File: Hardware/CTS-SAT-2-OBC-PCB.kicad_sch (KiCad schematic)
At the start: 0 parts

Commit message: Small updates
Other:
- removed sheet Temperature Sensor
- sheet STM32 ports: added none; removed DEBUG_LED, I2C4_SCL, I2C4_SDA
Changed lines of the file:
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@@
-	(wire
-		(pts
-			(xy 203.2 101.6) (xy 214.63 101.6)
-		)
-		(stroke
-			(width 0)
-			(type default)
-		)
-	)
 	(wire
 		(pts
@@
 		(pts
 			(xy 203.2 78.74) (xy 248.92 78.74)
-		)
-		(stroke
-			(width 0)
-			(type default)
-		)
-	)
-	(wire
-		(pts
-			(xy 203.2 99.06) (xy 214.63 99.06)
 		)
 		(stroke
@@
 	)
 	(sheet
-		(at 214.63 91.44)
-		(size 20.32 19.05)
-		(exclude_from_sim no)
-		(in_bom yes)
-		(on_board yes)
-		(dnp no)
-		(fields_autoplaced yes)
-		(stroke
-			(width 0.1524)
-			(type solid)
-		)
-		(fill
-			(color 0 0 0 0.0000)
-		)
-		(property "Sheetname" "Temperature Sensor"
-			(at 214.63 90.7284 0)
-			(effects
-				(font
-					(size 1.27 1.27)
-				)
-				(justify left bottom)
-			)
-		)
-		(property "Sheetfile" "temperature_sensor.kicad_sch"
-			(at 214.63 111.0746 0)
-			(effects
-				(font
-					(size 1.27 1.27)
-				)
-				(justify left top)
-			)
-		)
-		(pin "TEMP_SENS_SDA" bidirectional
-			(at 214.63 99.06 180)
-			(effects
-				(font
-					(size 1.27 1.27)
-				)
-				(justify left)
-			)
-		)
-		(pin "TEMP_SENS_SCL" bidirectional
-			(at 214.63 101.6 180)
-			(effects
-				(font
-					(size 1.27 1.27)
-				)
-				(justify left)
-			)
-		)
-		(instances
-			(project "CTS-SAT-2-OBC-PCB"
-				(path "/58243925-df8d-4fc1-899e-fce866d1d25a"
-					(page "5")
-				)
-			)
-		)
-	)
-	(sheet
 		(at 248.92 67.31)
 		(size 30.48 27.94)
@@
 			)
 		)
-		(pin "I2C4_SCL" bidirectional
-			(at 203.2 101.6 0)
-			(effects
-				(font
-					(size 1.27 1.27)
-				)
-				(justify right)
-			)
-		)
-		(pin "I2C4_SDA" bidirectional
-			(at 203.2 99.06 0)
-			(effects
-				(font
-					(size 1.27 1.27)
-				)
-				(justify right)
-			)
-		)
 		(pin "SPI2_MOSI" bidirectional
 			(at 144.78 99.06 180)
@@
 			(effects
 				(font
-					(size 1.27 1.27)
-				)
-				(justify left)
-			)
-		)
-		(pin "DEBUG_LED" output
-			(at 144.78 132.08 180)
-			(effects
-				(font

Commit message: RP2040 Schematic
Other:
- sheet PC104 Headers ports: added none; removed V_BAT
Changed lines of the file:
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@@
-			)
-		)
-		(pin "V_BAT" input
-			(at 279.4 90.17 0)
-			(effects
-				(font
-					(size 1.27 1.27)
-				)
-				(justify right)
 			)
 		)

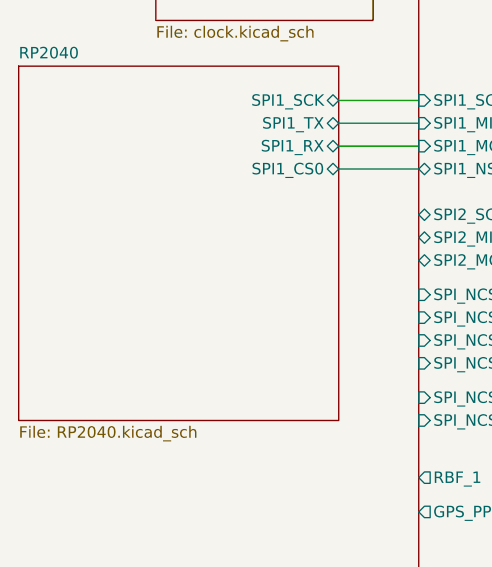
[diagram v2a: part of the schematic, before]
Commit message: Add fast clock
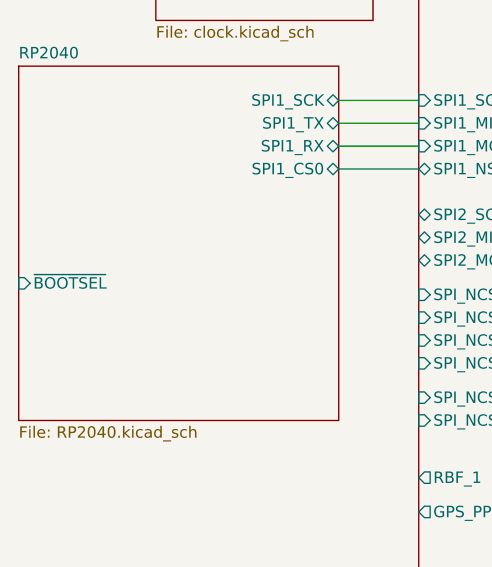
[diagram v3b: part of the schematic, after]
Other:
- sheet RP2040 ports: added ~{BOOTSEL}; removed none
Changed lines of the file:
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@@
+			)
+		)
+		(pin "~{BOOTSEL}" input
+			(at 100.33 101.6 180)
+			(effects
+				(font
+					(size 1.27 1.27)
+				)
+				(justify left)
 			)
 		)

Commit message: minor fix
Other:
- removed sheet Clock
- sheet STM32 ports: added none; removed BOOT0, OSC_IN
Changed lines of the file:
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@@
-	(wire
-		(pts
-			(xy 139.7 64.77) (xy 144.78 64.77)
-		)
-		(stroke
-			(width 0)
-			(type default)
-		)
-	)
 	(wire
 		(pts
@@
 			(width 0)
 			(type default)
-		)
-	)
-	(wire
-		(pts
-			(xy 139.7 62.23) (xy 144.78 62.23)
-		)
-		(stroke
-			(width 0)
-			(type default)
-		)
-	)
-	(sheet
-		(at 115.57 55.88)
-		(size 24.13 16.51)
-		(exclude_from_sim no)
-		(in_bom yes)
-		(on_board yes)
-		(dnp no)
-		(fields_autoplaced yes)
-		(stroke
-			(width 0.1524)
-			(type solid)
-		)
-		(fill
-			(color 0 0 0 0.0000)
-		)
-		(property "Sheetname" "Clock"
-			(at 115.57 55.1684 0)
-			(effects
-				(font
-					(size 1.27 1.27)
-				)
-				(justify left bottom)
-			)
-		)
-		(property "Sheetfile" "clock.kicad_sch"
-			(at 115.57 72.9746 0)
-			(effects
-				(font
-					(size 1.27 1.27)
-				)
-				(justify left top)
-			)
-		)
-		(pin "BOOT0" output
-			(at 139.7 62.23 0)
-			(effects
-				(font
-					(size 1.27 1.27)
-				)
-				(justify right)
-			)
-		)
-		(pin "OSC_IN" output
-			(at 139.7 64.77 0)
-			(effects
-				(font
-					(size 1.27 1.27)
-				)
-				(justify right)
-			)
-		)
-		(pin "OSC32_IN" output
-			(at 139.7 67.31 0)
-			(effects
-				(font
-					(size 1.27 1.27)
-				)
-				(justify right)
-			)
-		)
-		(pin "NRST" output
-			(at 139.7 59.69 0)
-			(effects
-				(font
-					(size 1.27 1.27)
-				)
-				(justify right)
-			)
-		)
-		(instances
-			(project "CTS-SAT-2-OBC-PCB"
-				(path "/58243925-df8d-4fc1-899e-fce866d1d25a"
-					(page "6")
-				)
-			)
 		)
 	)
@@
 			)
 		)
-		(pin "BOOT0" input
-			(at 144.78 62.23 180)
-			(effects
-				(font
-					(size 1.27 1.27)
-				)
-				(justify left)
-			)
-		)
 		(pin "NRST" input
 			(at 144.78 59.69 180)
@@
 			(effects
 				(font
-					(size 1.27 1.27)
-				)
-				(justify left)
-			)
-		)
-		(pin "OSC_IN" input
-			(at 144.78 64.77 180)
-			(effects
-				(font

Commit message: STM32 RTC
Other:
- added sheet Flash Memory (stm32_flash.kicad_sch)
- sheet STM32 ports: added none; removed OSC32_IN
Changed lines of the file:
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@@
+	(wire
+		(pts
+			(xy 130.81 102.87) (xy 144.78 102.87)
+		)
+		(stroke
+			(width 0)
+			(type default)
+		)
+	)
 	(wire
 		(pts
@@
 	(wire
 		(pts
+			(xy 130.81 105.41) (xy 144.78 105.41)
+		)
+		(stroke
+			(width 0)
+			(type default)
+		)
+	)
+	(wire
+		(pts
 			(xy 138.43 168.91) (xy 288.29 168.91)
 		)
@@
 	(wire
 		(pts
-			(xy 135.89 88.9) (xy 144.78 88.9)
+			(xy 97.79 81.28) (xy 144.78 81.28)
+		)
+		(stroke
+			(width 0)
+			(type default)
+		)
+	)
+	(wire
+		(pts
+			(xy 130.81 110.49) (xy 144.78 110.49)
 		)
 		(stroke
@@
 	(wire
 		(pts
-			(xy 135.89 86.36) (xy 144.78 86.36)
-		)
-		(stroke
-			(width 0)
-			(type default)
-		)
-	)
-	(wire
-		(pts
-			(xy 139.7 67.31) (xy 144.78 67.31)
-		)
-		(stroke
-			(width 0)
-			(type default)
-		)
-	)
-	(wire
-		(pts
-			(xy 135.89 81.28) (xy 144.78 81.28)
+			(xy 97.79 78.74) (xy 144.78 78.74)
+		)
+		(stroke
+			(width 0)
+			(type default)
+		)
+	)
+	(wire
+		(pts
+			(xy 97.79 73.66) (xy 144.78 73.66)
 		)
 		(stroke
@@
 	(wire
 		(pts
-			(xy 135.89 83.82) (xy 144.78 83.82)
+			(xy 130.81 107.95) (xy 144.78 107.95)
+		)
+		(stroke
+			(width 0)
+			(type default)
+		)
+	)
+	(wire
+		(pts
+			(xy 97.79 76.2) (xy 144.78 76.2)
 		)
 		(stroke
@@
 			(width 0)
 			(type default)
+		)
+	)
+	(wire
+		(pts
+			(xy 130.81 96.52) (xy 144.78 96.52)
+		)
+		(stroke
+			(width 0)
+			(type default)
+		)
+	)
+	(wire
+		(pts
+			(xy 130.81 93.98) (xy 144.78 93.98)
+		)
+		(stroke
+			(width 0)
+			(type default)
+		)
+	)
+	(wire
+		(pts
+			(xy 130.81 99.06) (xy 144.78 99.06)
+		)
+		(stroke
+			(width 0)
+			(type default)
+		)
+	)
+	(sheet
+		(at 109.22 91.44)
+		(size 21.59 22.86)
+		(exclude_from_sim no)
+		(in_bom yes)
+		(on_board yes)
+		(dnp no)
+		(fields_autoplaced yes)
+		(stroke
+			(width 0.1524)
+			(type solid)
+		)
+		(fill
+			(color 0 0 0 0.0000)
+		)
+		(property "Sheetname" "Flash Memory"
+			(at 109.22 90.7284 0)
+			(effects
+				(font
+					(size 1.27 1.27)
+				)
+				(justify left bottom)
+			)
+		)
+		(property "Sheetfile" "stm32_flash.kicad_sch"
+			(at 109.22 114.8846 0)
+			(effects
+				(font
+					(size 1.27 1.27)
+				)
+				(justify left top)
+				(hide yes)
+			)
+		)
+		(pin "SPI_NCS_FLASH_3" input
+			(at 130.81 110.49 0)
+			(effects
+				(font
+					(size 1.27 1.27)
+				)
+				(justify right)
+			)
+		)
+		(pin "SPI_FLASH_MISO" output
+			(at 130.81 96.52 0)
+			(effects
+				(font
+					(size 1.27 1.27)
+				)
+				(justify right)
+			)
+		)
+		(pin "SPI_NCS_FLASH_1" input
+			(at 130.81 105.41 0)
+			(effects
+				(font
+					(size 1.27 1.27)
+				)
+				(justify right)
+			)
+		)
+		(pin "SPI_FLASH_SCLK" output
+			(at 130.81 93.98 0)
+			(effects
+				(font
+					(size 1.27 1.27)
+				)
+				(justify right)
+			)
+		)
+		(pin "SPI_NCS_FLASH_2" input
+			(at 130.81 107.95 0)
+			(effects
+				(font
+					(size 1.27 1.27)
+				)
+				(justify right)
+			)
+		)
+		(pin "SPI_FLASH_MOSI" output
+			(at 130.81 99.06 0)
+			(effects
+				(font
+					(size 1.27 1.27)
+				)
+				(justify right)
+			)
+		)
+		(pin "SPI_NCS_FLASH_0" input
+			(at 130.81 102.87 0)
+			(effects
+				(font
+					(size 1.27 1.27)
+				)
+				(justify right)
+			)
+		)
+		(instances
+			(project "CTS-SAT-2-OBC-PCB"
+				(path "/58243925-df8d-4fc1-899e-fce866d1d25a"
+					(page "5")
+				)
+			)
 		)
 	)
@@
 	)
 	(sheet
-		(at 100.33 77.47)
-		(size 35.56 39.37)
+		(at 62.23 66.04)
+		(size 35.56 21.59)
 		(exclude_from_sim no)
 		(in_bom yes)
@@
 		)
 		(property "Sheetname" "RP2040"
-			(at 100.33 76.7584 0)
+			(at 62.23 65.3284 0)
 			(effects
 				(font
@@
 		)
 		(property "Sheetfile" "RP2040.kicad_sch"
-			(at 100.33 117.4246 0)
+			(at 62.23 88.2146 0)
 			(effects
 				(font
@@
 				)
 				(justify left top)
+				(hide yes)
 			)
 		)
 		(pin "SPI1_RX" bidirectional
-			(at 135.89 86.36 0)
+			(at 97.79 78.74 0)
 			(effects
 				(font
@@
 		)
 		(pin "SPI1_CS0" bidirectional
-			(at 135.89 88.9 0)
+			(at 97.79 81.28 0)
 			(effects
 				(font
@@
 		)
 		(pin "SPI1_TX" bidirectional
-			(at 135.89 83.82 0)
+			(at 97.79 76.2 0)
 			(effects
 				(font
@@
 		)
 		(pin "SPI1_SCK" bidirectional
-			(at 135.89 81.28 0)
+			(at 97.79 73.66 0)
 			(effects
 				(font
@@
 		)
 		(pin "~{BOOTSEL}" input
-			(at 100.33 101.6 180)
+			(at 62.23 72.39 180)
 			(effects
 				(font
@@
 		)
 		(pin "SPI1_MOSI" input
-			(at 144.78 86.36 180)
+			(at 144.78 78.74 180)
 			(effects
 				(font
@@
 		)
 		(pin "SPI1_MISO" input
-			(at 144.78 83.82 180)
+			(at 144.78 76.2 180)
 			(effects
 				(font
@@
 		)
 		(pin "SPI1_SCLK" input
-			(at 144.78 81.28 180)
+			(at 144.78 73.66 180)
 			(effects
 				(font
@@
 			)
 		)
-		(pin "OSC32_IN" input
-			(at 144.78 67.31 180)
-			(effects
-				(font
-					(size 1.27 1.27)
-				)
-				(justify left)
-			)
-		)
 		(pin "SPI1_NSS" bidirectional
-			(at 144.78 88.9 180)
-			(effects
-				(font
+			(at 144.78 81.28 180)
+			(effects
+				(font

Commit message: prepare for FRAM
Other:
- sheet Flash Memory renamed Memory
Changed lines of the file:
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@@
 			(color 0 0 0 0.0000)
 		)
-		(property "Sheetname" "Flash Memory"
+		(property "Sheetname" "Memory"
 			(at 109.22 90.7284 0)
 			(effects
@@
 		)
 		(pin "BOOM_CTRL_1" output
-			(at 144.78 140.97 180)
+			(at 144.78 143.51 180)
 			(effects
 				(font
@@
 		)
 		(pin "BOOM_CTRL_2" output
-			(at 144.78 143.51 180)
-			(effects
-				(font
+			(at 144.78 146.05 180)
+			(effects
+				(font

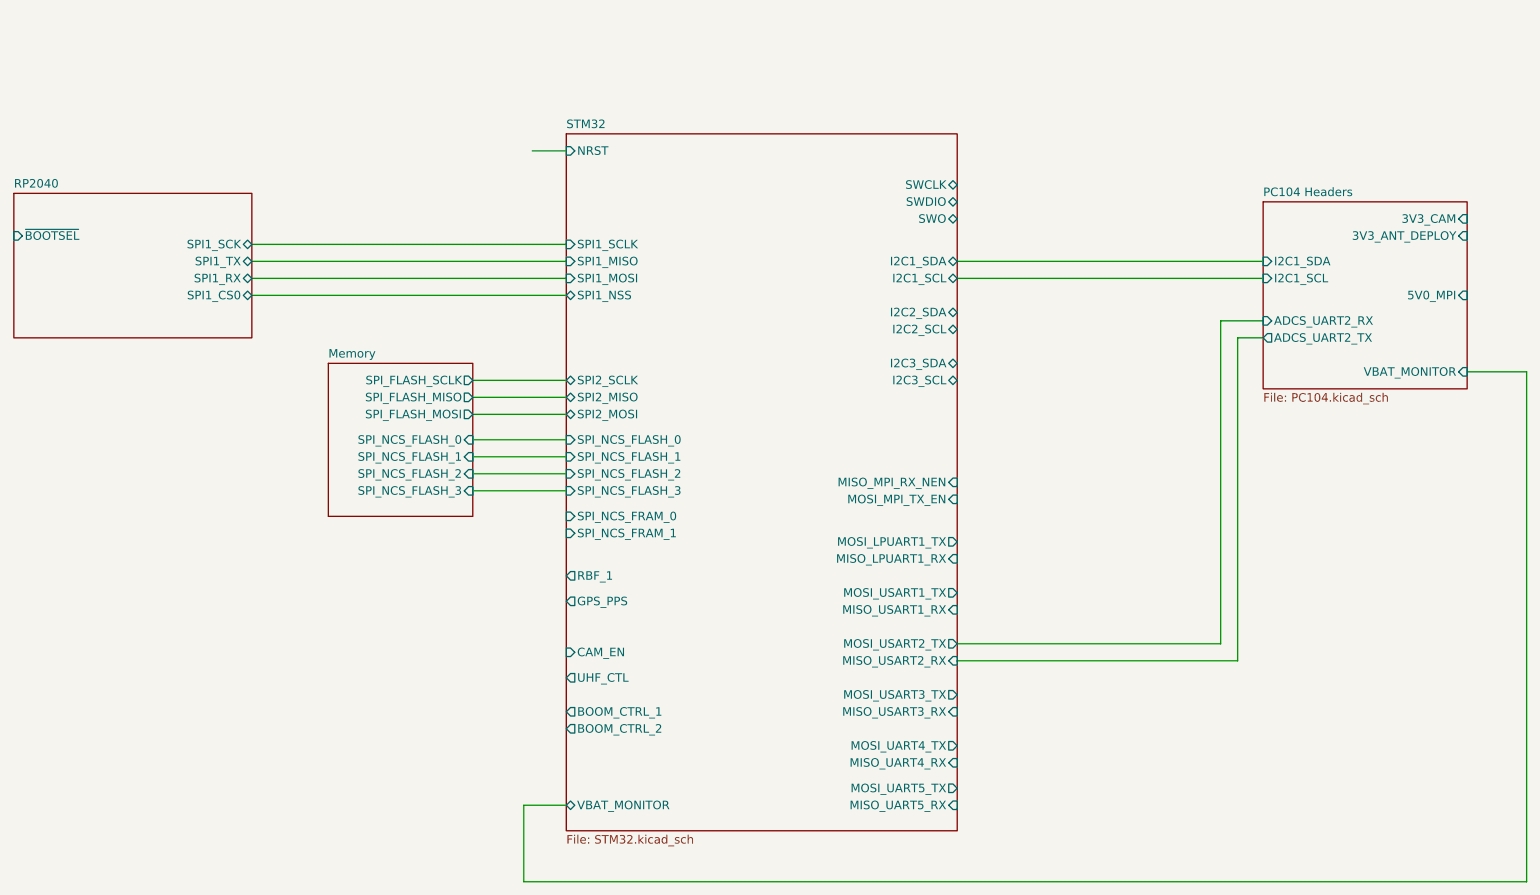
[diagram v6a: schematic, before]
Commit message: Begin with connectors
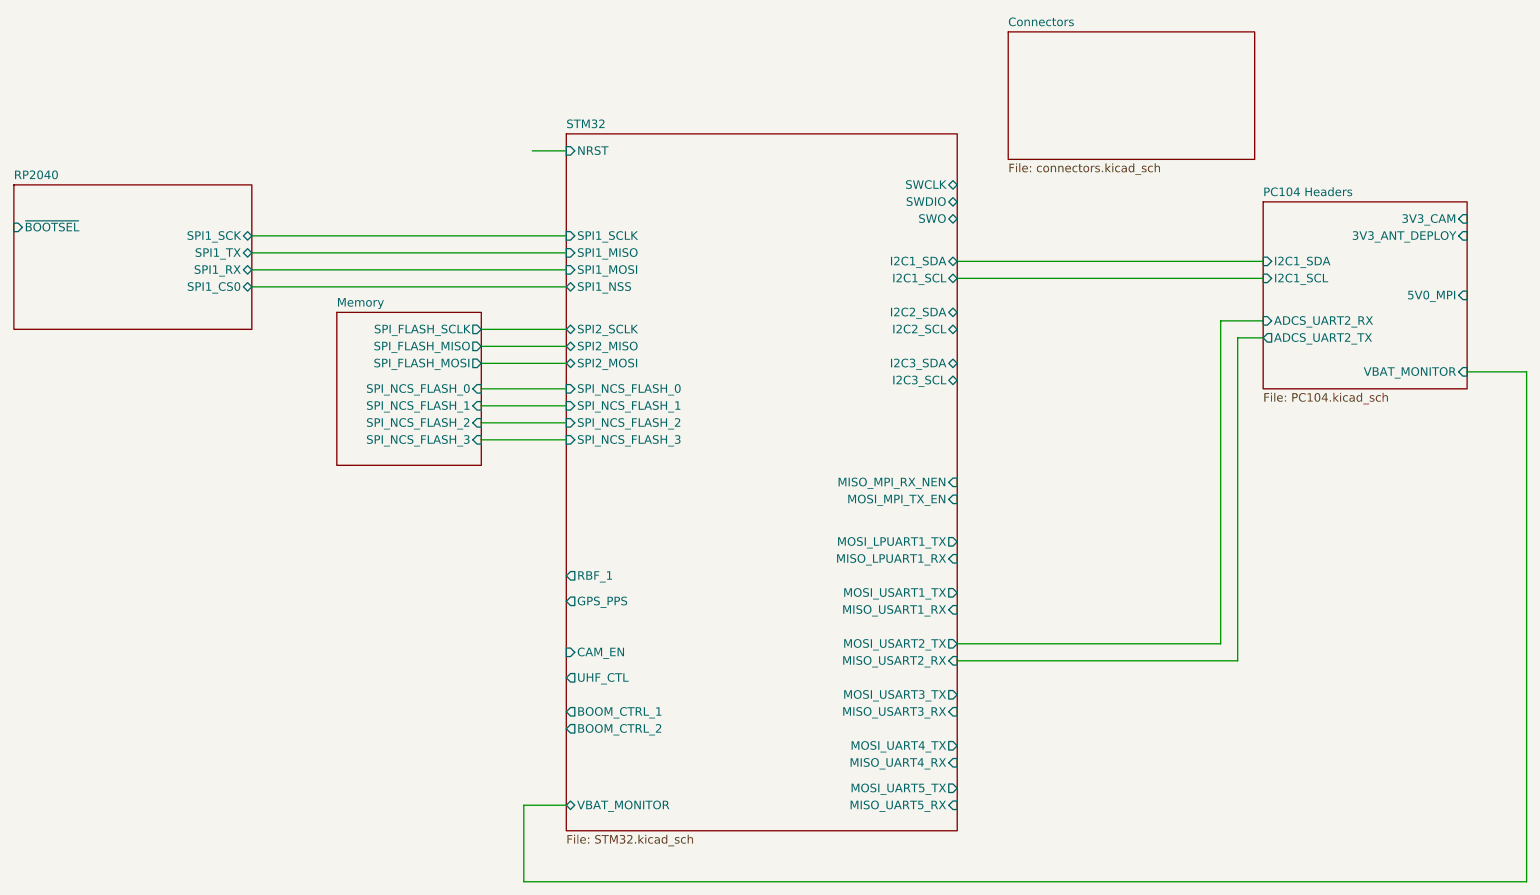
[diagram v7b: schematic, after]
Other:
- added sheet Connectors (connectors.kicad_sch)
- sheet STM32 ports: added none; removed SPI_NCS_FRAM_0, SPI_NCS_FRAM_1
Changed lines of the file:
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@@
 	(wire
 		(pts
-			(xy 130.81 102.87) (xy 144.78 102.87)
+			(xy 132.08 95.25) (xy 144.78 95.25)
 		)
 		(stroke
@@
 	(wire
 		(pts
-			(xy 130.81 105.41) (xy 144.78 105.41)
+			(xy 132.08 97.79) (xy 144.78 97.79)
 		)
 		(stroke
@@
 	(wire
 		(pts
-			(xy 97.79 81.28) (xy 144.78 81.28)
-		)
-		(stroke
-			(width 0)
-			(type default)
-		)
-	)
-	(wire
-		(pts
-			(xy 130.81 110.49) (xy 144.78 110.49)
+			(xy 97.79 80.01) (xy 144.78 80.01)
+		)
+		(stroke
+			(width 0)
+			(type default)
+		)
+	)
+	(wire
+		(pts
+			(xy 132.08 102.87) (xy 144.78 102.87)
 		)
 		(stroke
@@
 	(wire
 		(pts
-			(xy 97.79 78.74) (xy 144.78 78.74)
-		)
-		(stroke
-			(width 0)
-			(type default)
-		)
-	)
-	(wire
-		(pts
-			(xy 97.79 73.66) (xy 144.78 73.66)
+			(xy 97.79 77.47) (xy 144.78 77.47)
+		)
+		(stroke
+			(width 0)
+			(type default)
+		)
+	)
+	(wire
+		(pts
+			(xy 97.79 72.39) (xy 144.78 72.39)
 		)
 		(stroke
@@
 	(wire
 		(pts
-			(xy 130.81 107.95) (xy 144.78 107.95)
-		)
-		(stroke
-			(width 0)
-			(type default)
-		)
-	)
-	(wire
-		(pts
-			(xy 97.79 76.2) (xy 144.78 76.2)
+			(xy 132.08 100.33) (xy 144.78 100.33)
+		)
+		(stroke
+			(width 0)
+			(type default)
+		)
+	)
+	(wire
+		(pts
+			(xy 97.79 74.93) (xy 144.78 74.93)
 		)
 		(stroke
@@
 	(wire
 		(pts
-			(xy 130.81 96.52) (xy 144.78 96.52)
-		)
-		(stroke
-			(width 0)
-			(type default)
-		)
-	)
-	(wire
-		(pts
-			(xy 130.81 93.98) (xy 144.78 93.98)
-		)
-		(stroke
-			(width 0)
-			(type default)
-		)
-	)
-	(wire
-		(pts
-			(xy 130.81 99.06) (xy 144.78 99.06)
+			(xy 132.08 88.9) (xy 144.78 88.9)
+		)
+		(stroke
+			(width 0)
+			(type default)
+		)
+	)
+	(wire
+		(pts
+			(xy 132.08 86.36) (xy 144.78 86.36)
+		)
+		(stroke
+			(width 0)
+			(type default)
+		)
+	)
+	(wire
+		(pts
+			(xy 132.08 91.44) (xy 144.78 91.44)
 		)
 		(stroke
@@
 	)
 	(sheet
-		(at 109.22 91.44)
+		(at 110.49 83.82)
 		(size 21.59 22.86)
 		(exclude_from_sim no)
@@
 		)
 		(property "Sheetname" "Memory"
-			(at 109.22 90.7284 0)
+			(at 110.49 83.1084 0)
 			(effects
 				(font
@@
 		)
 		(property "Sheetfile" "stm32_flash.kicad_sch"
-			(at 109.22 114.8846 0)
+			(at 110.49 107.2646 0)
 			(effects
 				(font
@@
 		)
 		(pin "SPI_NCS_FLASH_3" input
-			(at 130.81 110.49 0)
+			(at 132.08 102.87 0)
 			(effects
 				(font
@@
 		)
 		(pin "SPI_FLASH_MISO" output
-			(at 130.81 96.52 0)
+			(at 132.08 88.9 0)
 			(effects
 				(font
@@
 		)
 		(pin "SPI_NCS_FLASH_1" input
-			(at 130.81 105.41 0)
+			(at 132.08 97.79 0)
 			(effects
 				(font
@@
 		)
 		(pin "SPI_FLASH_SCLK" output
-			(at 130.81 93.98 0)
+			(at 132.08 86.36 0)
 			(effects
 				(font
@@
 		)
 		(pin "SPI_NCS_FLASH_2" input
-			(at 130.81 107.95 0)
+			(at 132.08 100.33 0)
 			(effects
 				(font
@@
 		)
 		(pin "SPI_FLASH_MOSI" output
-			(at 130.81 99.06 0)
+			(at 132.08 91.44 0)
 			(effects
 				(font
@@
 		)
 		(pin "SPI_NCS_FLASH_0" input
-			(at 130.81 102.87 0)
+			(at 132.08 95.25 0)
 			(effects
 				(font
@@
 	)
 	(sheet
-		(at 62.23 66.04)
+		(at 62.23 64.77)
 		(size 35.56 21.59)
 		(exclude_from_sim no)
@@
 		)
 		(property "Sheetname" "RP2040"
-			(at 62.23 65.3284 0)
+			(at 62.23 64.0584 0)
 			(effects
 				(font
@@
 		)
 		(property "Sheetfile" "RP2040.kicad_sch"
-			(at 62.23 88.2146 0)
+			(at 62.23 86.9446 0)
 			(effects
 				(font
@@
 		)
 		(pin "SPI1_RX" bidirectional
-			(at 97.79 78.74 0)
+			(at 97.79 77.47 0)
 			(effects
 				(font
@@
 		)
 		(pin "SPI1_CS0" bidirectional
-			(at 97.79 81.28 0)
+			(at 97.79 80.01 0)
 			(effects
 				(font
@@
 		)
 		(pin "SPI1_TX" bidirectional
-			(at 97.79 76.2 0)
+			(at 97.79 74.93 0)
 			(effects
 				(font
@@
 		)
 		(pin "SPI1_SCK" bidirectional
-			(at 97.79 73.66 0)
+			(at 97.79 72.39 0)
 			(effects
 				(font
@@
 		)
 		(pin "~{BOOTSEL}" input
-			(at 62.23 72.39 180)
+			(at 62.23 71.12 180)
 			(effects
 				(font
@@
 		)
 		(pin "SPI2_MOSI" bidirectional
-			(at 144.78 99.06 180)
+			(at 144.78 91.44 180)
 			(effects
 				(font
@@
 		)
 		(pin "SPI2_MISO" bidirectional
-			(at 144.78 96.52 180)
+			(at 144.78 88.9 180)
 			(effects
 				(font
@@
 		)
 		(pin "SPI2_SCLK" bidirectional
-			(at 144.78 93.98 180)
+			(at 144.78 86.36 180)
 			(effects
 				(font
@@
 		)
 		(pin "SPI_NCS_FLASH_3" input
-			(at 144.78 110.49 180)
-			(effects
-				(font
-					(size 1.27 1.27)
-				)
-				(justify left)
-			)
-		)
-		(pin "SPI_NCS_FRAM_0" input
-			(at 144.78 114.3 180)
+			(at 144.78 102.87 180)
 			(effects
 				(font
@@
 		)
 		(pin "SPI_NCS_FLASH_0" input
-			(at 144.78 102.87 180)
+			(at 144.78 95.25 180)
 			(effects
 				(font
@@
 		)
 		(pin "SPI_NCS_FLASH_2" input
-			(at 144.78 107.95 180)
+			(at 144.78 100.33 180)
 			(effects
 				(font
@@
 		)
 		(pin "SPI_NCS_FLASH_1" input
-			(at 144.78 105.41 180)
-			(effects
-				(font
-					(size 1.27 1.27)
-				)
-				(justify left)
-			)
-		)
-		(pin "SPI_NCS_FRAM_1" input
-			(at 144.78 116.84 180)
+			(at 144.78 97.79 180)
 			(effects
 				(font
@@
 		)
 		(pin "SPI1_MOSI" input
-			(at 144.78 78.74 180)
+			(at 144.78 77.47 180)
 			(effects
 				(font
@@
 		)
 		(pin "SPI1_MISO" input
-			(at 144.78 76.2 180)
+			(at 144.78 74.93 180)
 			(effects
 				(font
@@
 		)
 		(pin "SPI1_SCLK" input
-			(at 144.78 73.66 180)
+			(at 144.78 72.39 180)
 			(effects
 				(font
@@
 		)
 		(pin "SPI1_NSS" bidirectional
-			(at 144.78 81.28 180)
+			(at 144.78 80.01 180)
 			(effects
 				(font
@@
 				)
 			)
+		)
+	)
+	(sheet
+		(at 210.82 41.91)
+		(size 36.83 19.05)
+		(exclude_from_sim no)
+		(in_bom yes)
+		(on_board yes)
+		(dnp no)
+		(fields_autoplaced yes)
+		(stroke
+			(width 0.1524)
+			(type solid)
+		)
+		(fill
+			(color 0 0 0 0.0000)
+		)
+		(property "Sheetname" "Connectors"
+			(at 210.82 41.1984 0)
+			(effects
+				(font
+					(size 1.27 1.27)
+				)
+				(justify left bottom)
+			)
+		)
+		(property "Sheetfile" "connectors.kicad_sch"
+			(at 210.82 61.5446 0)
+			(effects
+				(font
+					(size 1.27 1.27)
+				)
+				(justify left top)
+			)
+		)
+		(instances
+			(project "CTS-SAT-2-OBC-PCB"
+				(path "/58243925-df8d-4fc1-899e-fce866d1d25a"
+					(page "6")
+				)
+			)
